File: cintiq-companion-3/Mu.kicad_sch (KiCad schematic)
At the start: 12 parts, among them J1 Conn_01x03_Pin

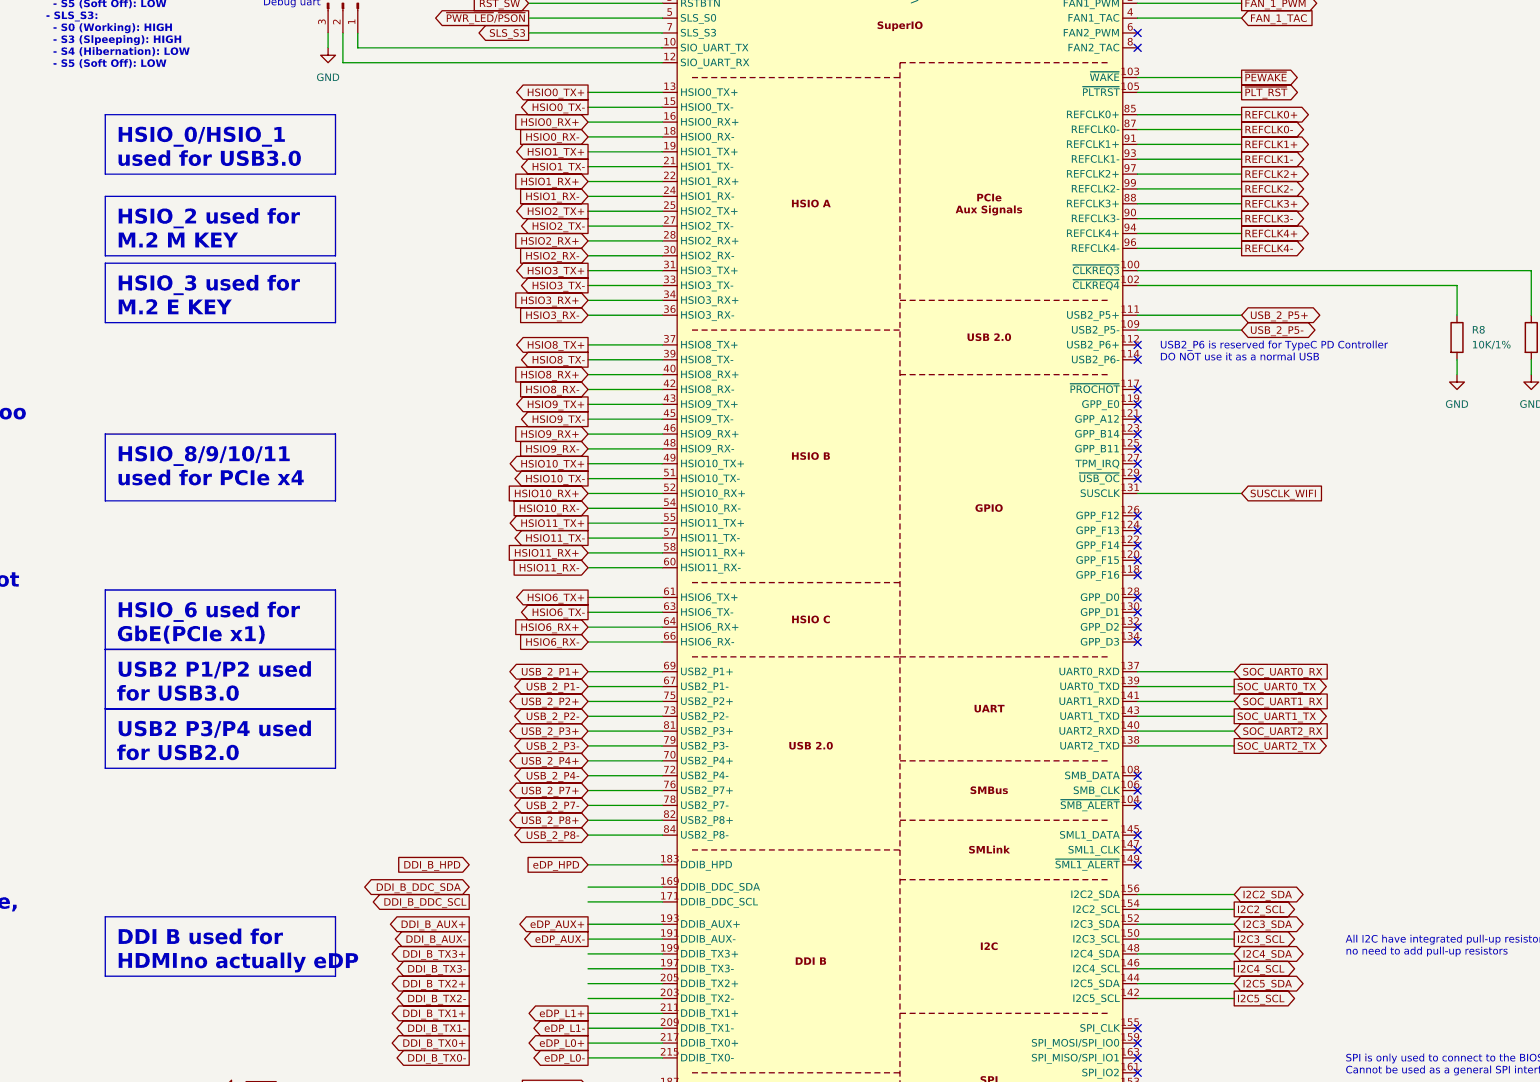
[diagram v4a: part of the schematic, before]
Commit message: Added E-key slot
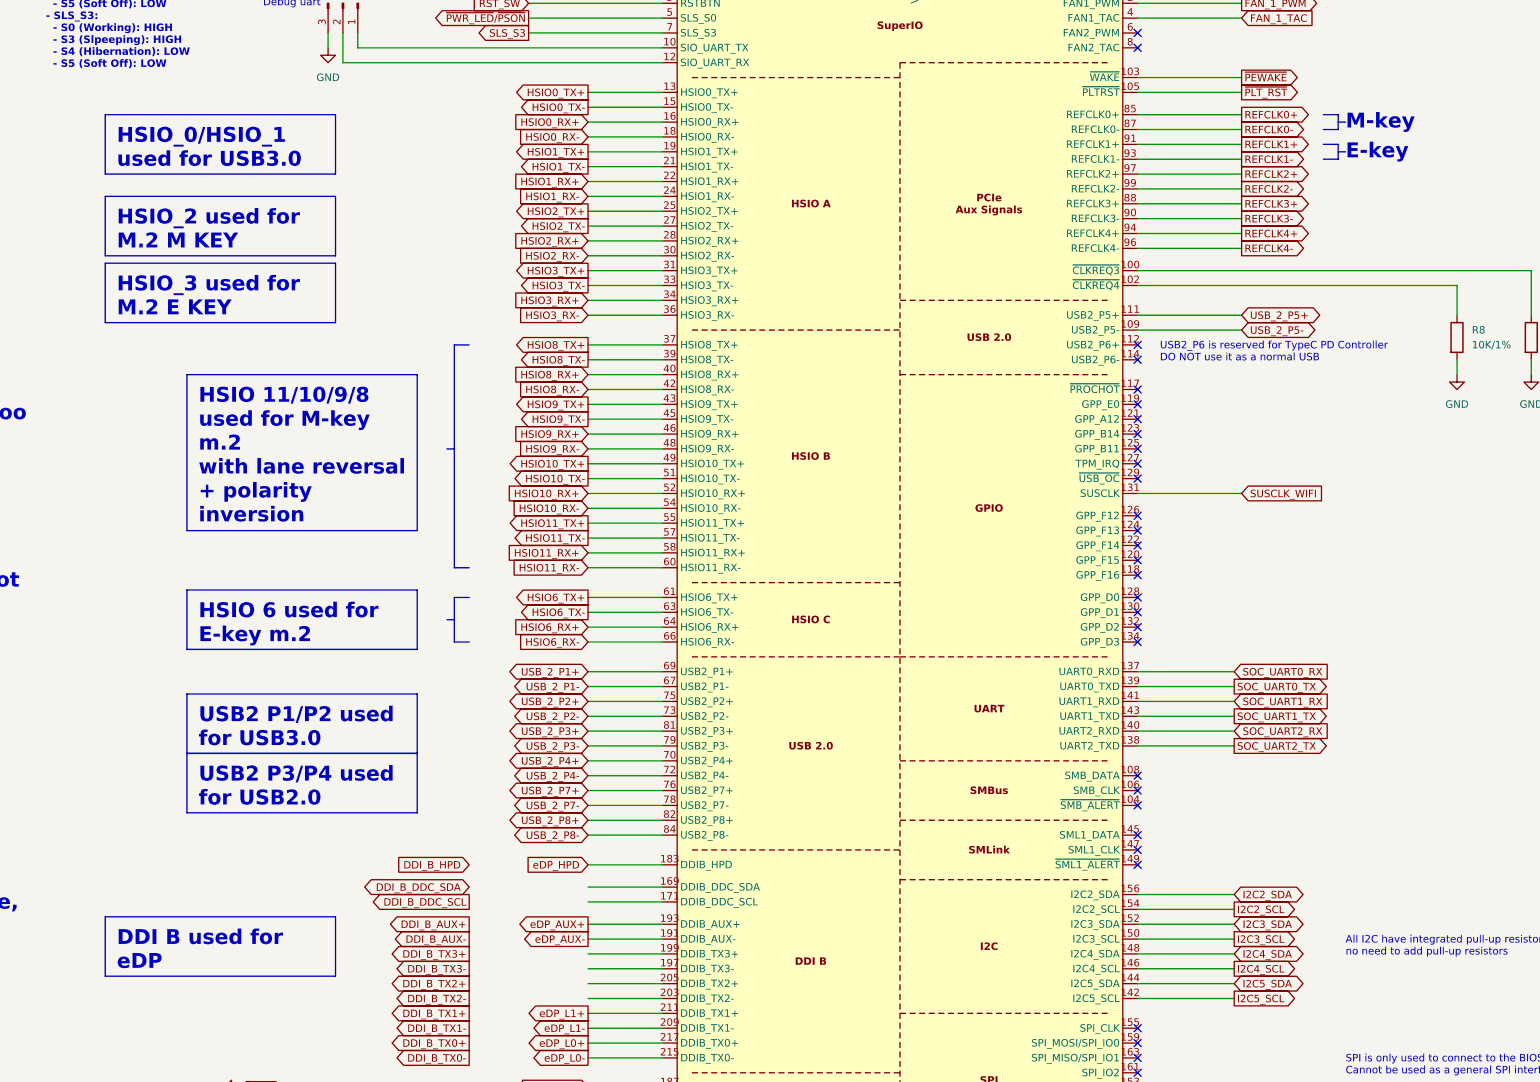
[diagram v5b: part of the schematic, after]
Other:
- note added: "E-key"
- note added: "M-key"
- note removed: "no actually eDP"
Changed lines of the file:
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@@
 		)
 	)
+	(polyline
+		(pts
+			(xy 462.28 93.98) (xy 462.28 96.52)
+		)
+		(stroke
+			(width 0)
+			(type default)
+		)
+	)
 	(wire
 		(pts
@@
 		)
 	)
+	(polyline
+		(pts
+			(xy 462.28 100.33) (xy 463.55 100.33)
+		)
+		(stroke
+			(width 0)
+			(type default)
+		)
+	)
 	(wire
 		(pts
@@
 		)
 	)
+	(polyline
+		(pts
+			(xy 311.15 133.35) (xy 311.15 171.45)
+		)
+		(stroke
+			(width 0)
+			(type default)
+		)
+	)
 	(wire
 		(pts
@@
 		)
 	)
+	(polyline
+		(pts
+			(xy 313.69 176.53) (xy 311.15 176.53)
+		)
+		(stroke
+			(width 0)
+			(type default)
+		)
+	)
 	(wire
 		(pts
@@
 		)
 	)
+	(polyline
+		(pts
+			(xy 313.69 133.35) (xy 311.15 133.35)
+		)
+		(stroke
+			(width 0)
+			(type default)
+		)
+	)
 	(wire
 		(pts
@@
 		)
 	)
+	(polyline
+		(pts
+			(xy 311.15 180.34) (xy 309.88 180.34)
+		)
+		(stroke
+			(width 0)
+			(type default)
+		)
+	)
 	(wire
 		(pts
@@
 		)
 	)
+	(polyline
+		(pts
+			(xy 462.28 95.25) (xy 463.55 95.25)
+		)
+		(stroke
+			(width 0)
+			(type default)
+		)
+	)
 	(wire
 		(pts
@@
 		)
 	)
+	(polyline
+		(pts
+			(xy 459.74 93.98) (xy 462.28 93.98)
+		)
+		(stroke
+			(width 0)
+			(type default)
+		)
+	)
 	(wire
 		(pts
@@
 		)
 	)
+	(polyline
+		(pts
+			(xy 313.69 171.45) (xy 311.15 171.45)
+		)
+		(stroke
+			(width 0)
+			(type default)
+		)
+	)
 	(wire
 		(pts
@@
 		)
 	)
+	(polyline
+		(pts
+			(xy 313.69 184.15) (xy 311.15 184.15)
+		)
+		(stroke
+			(width 0)
+			(type default)
+		)
+	)
 	(wire
 		(pts
@@
 		)
 	)
+	(polyline
+		(pts
+			(xy 459.74 101.6) (xy 462.28 101.6)
+		)
+		(stroke
+			(width 0)
+			(type default)
+		)
+	)
 	(wire
 		(pts
@@
 		)
 	)
+	(polyline
+		(pts
+			(xy 311.15 176.53) (xy 311.15 184.15)
+		)
+		(stroke
+			(width 0)
+			(type default)
+		)
+	)
+	(polyline
+		(pts
+			(xy 462.28 99.06) (xy 462.28 101.6)
+		)
+		(stroke
+			(width 0)
+			(type default)
+		)
+	)
 	(wire
 		(pts
@@
 		)
 	)
+	(polyline
+		(pts
+			(xy 459.74 99.06) (xy 462.28 99.06)
+		)
+		(stroke
+			(width 0)
+			(type default)
+		)
+	)
 	(wire
 		(pts
@@
 		)
 	)
+	(polyline
+		(pts
+			(xy 459.74 96.52) (xy 462.28 96.52)
+		)
+		(stroke
+			(width 0)
+			(type default)
+		)
+	)
 	(wire
 		(pts
@@
 		)
 	)
+	(polyline
+		(pts
+			(xy 311.15 151.13) (xy 309.88 151.13)
+		)
+		(stroke
+			(width 0)
+			(type default)
+		)
+	)
 	(wire
 		(pts
@@
 		)
 	)
-	(text_box "DDI B used for HDMI"
+	(text_box "DDI B used for eDP"
 		(exclude_from_sim no)
 		(at 251.46 231.14 0)
@@
 				(thickness 0.508)
 				(bold yes)
+				(color 255 121 154 1)
 			)
 			(justify left top)
@@
 	(text_box "USB2 P3/P4 used for USB2.0 \n"
 		(exclude_from_sim no)
-		(at 251.46 195.58 0)
+		(at 265.43 203.2 0)
 		(size 39.37 10.16)
 		(stroke
@@
 		)
 	)
-	(text_box "HSIO_8/9/10/11 used for PCIe x4\n\n"
+	(text_box "HSIO 11/10/9/8 used for M-key m.2\nwith lane reversal + polarity inversion"
 		(exclude_from_sim no)
-		(at 251.46 148.59 0)
-		(size 39.37 11.43)
+		(at 265.43 138.43 0)
+		(size 39.37 26.67)
 		(stroke
 			(width 0)
@@
 				(thickness 0.508)
 				(bold yes)
+				(color 255 121 154 1)
 			)
 			(justify left top)
 		)
 	)
-	(text_box "HSIO_6 used for GbE(PCIe x1)\n"
+	(text_box "HSIO 6 used for E-key m.2"
 		(exclude_from_sim no)
-		(at 251.46 175.26 0)
+		(at 265.43 175.26 0)
 		(size 39.37 10.16)
 		(stroke
@@
 				(thickness 0.508)
 				(bold yes)
+				(color 255 121 154 1)
 			)
 			(justify left top)
@@
 	(text_box "USB2 P1/P2 used for USB3.0\n"
 		(exclude_from_sim no)
-		(at 251.46 185.42 0)
+		(at 265.43 193.04 0)
 		(size 39.37 10.16)
 		(stroke
@@
 		)
 	)
-	(text "no actually eDP\n"
-		(exclude_from_sim no)
-		(at 264.16 237.49 0)
-		(effects
-			(font
-				(size 2.54 2.54)
-				(thickness 0.508)
-				(bold yes)
-				(color 255 121 154 1)
-			)
-			(justify left top)
-		)
-	)
 	(text "HPD pin of unused DDI/TCP port\nneeds to be pulled down"
 		(exclude_from_sim no)
@@
 		)
 	)
+	(text "E-key"
+		(exclude_from_sim no)
+		(at 463.55 100.33 0)
+		(effects
+			(font
+				(size 2.54 2.54)
+				(thickness 0.508)
+				(bold yes)
+				(color 255 121 154 1)
+			)
+			(justify left)
+		)
+	)
 	(text "I got the flash image tool,\nso I should be able to change\nit to whatever I need :3"
 		(exclude_from_sim no)
@@
 		)
 	)
+	(text "M-key\n"
+		(exclude_from_sim no)
+		(at 463.55 95.25 0)
+		(effects
+			(font
+				(size 2.54 2.54)
+				(thickness 0.508)
+				(bold yes)
+				(color 255 121 154 1)
+			)
+			(justify left)
+		)
+	)

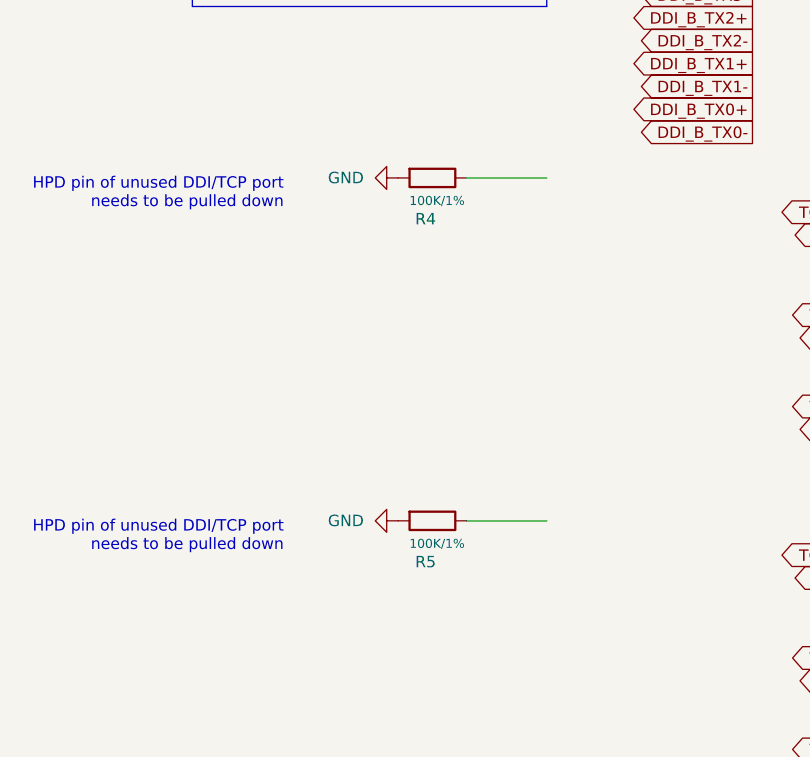
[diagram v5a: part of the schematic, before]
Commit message: Added ground fill
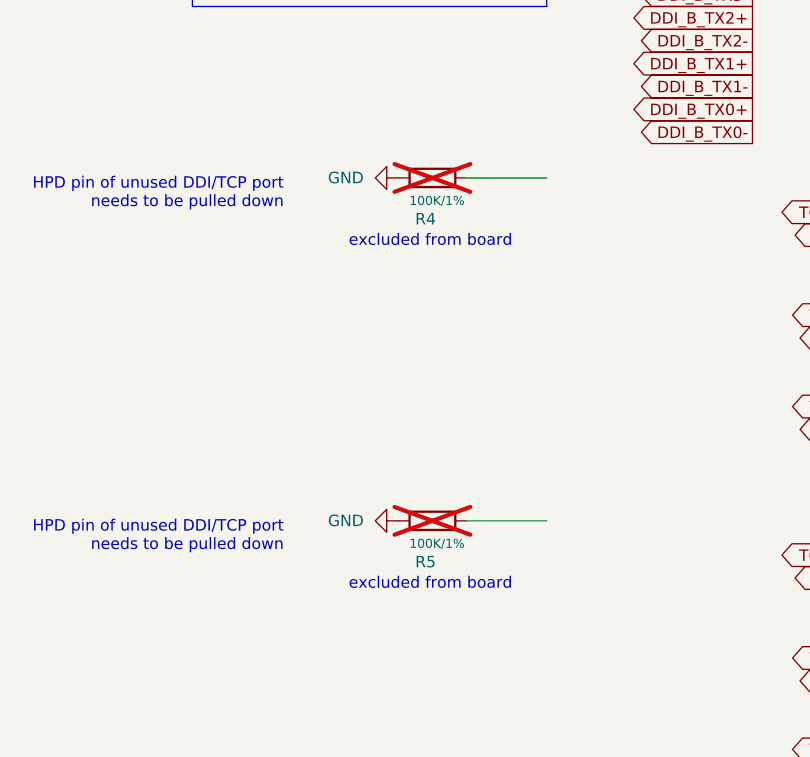
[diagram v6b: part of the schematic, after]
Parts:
- R4, R5: now not fitted
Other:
- note added: "excluded from board"
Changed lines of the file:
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@@
 		)
 	)
+	(text "excluded from board"
+		(exclude_from_sim no)
+		(at 287.02 304.8 0)
+		(effects
+			(font
+				(size 1.27 1.27)
+			)
+			(justify right top)
+		)
+	)
 	(text "Sleeping State Signal\n\n- SLS_S0: \n  - S0 (Working): HIGH\n  - S3 (Slpeeping): LOW\n  - S4 (Hibernation): LOW\n  - S5 (Soft Off): LOW\n- SLS_S3:\n  - S0 (Working): HIGH\n  - S3 (Slpeeping): HIGH\n  - S4 (Hibernation): LOW\n  - S5 (Soft Off): LOW"
 		(exclude_from_sim no)
@@
 		)
 	)
+	(text "excluded from board"
+		(exclude_from_sim no)
+		(at 287.02 266.7 0)
+		(effects
+			(font
+				(size 1.27 1.27)
+			)
+			(justify right top)
+		)
+	)
 	(text "All I2C have integrated pull-up resistors.\nno need to add pull-up resistors"
 		(exclude_from_sim no)
@@
 		(exclude_from_sim no)
 		(in_bom yes)
-		(on_board yes)
-		(dnp no)
+		(on_board no)
+		(dnp yes)
 		(property "Reference" "R4"
 			(at 277.368 264.922 90)
@@
 		(exclude_from_sim no)
 		(in_bom yes)
-		(on_board yes)
-		(dnp no)
+		(on_board no)
+		(dnp yes)
 		(property "Reference" "R5"
 			(at 277.368 303.022 90)
